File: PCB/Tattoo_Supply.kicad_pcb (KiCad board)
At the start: 4 copper layers, 95 x 128 mm, 140 parts, among them J1 Barrel_Jack_Switch, J2 Out_{1}, J3 Out_{2}, J4 USB_C_Receptacle_USB2.0, J5 Conn_ST_STDC14, J6 Debug_JTAG, J7 Debug_UART, J8 Footswitch, Q1 SiA441DJ, Q2 SSM6J507NU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

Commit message: routage en cours
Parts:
- moved R17 1.68 mm to (119.0, 78.8)
- moved R20 1.68 mm to (119.0, 80.2)
- moved R25 1.68 mm to (119.0, 77.2)
- moved FB1 1.60 mm to (139.2, 69.7), turned to -90 degrees
- moved C1 1.40 mm to (87.0, 62.8)
- moved D3 1.40 mm to (87.0, 61.0)
- moved C33 1.25 mm to (127.5, 116.0)
- moved R41 1.25 mm to (126.0, 116.0)
- moved R18 1.20 mm to (123.6, 77.7)
- moved R19 1.20 mm to (123.6, 79.2)
- moved R9 1.15 mm to (91.0, 73.2)
- moved C17 1.10 mm to (119.4, 68.0), turned to 90 degrees
- moved C31 0.93 mm to (126.0, 112.8), turned to -90 degrees
- moved C14 0.89 mm to (130.4, 62.4)
- moved C20 0.29 mm to (126.6, 78.0), turned to 180 degrees
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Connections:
- net Net-(#FLG01-pwr) renamed /USB C Power Delivery/VBUS_USB
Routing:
- net +3V3: track 0.00 -> 88.7 mm, vias 0 -> 23
- net GND: track 6.21 -> 58.4 mm, vias 3 -> 19
- net /USB C Power Delivery/VBUS_USB: track 2.46 -> 18.9 mm, vias 0 -> 8
- net /MCU/~{RESET}: track 0.00 -> 15.9 mm
- net /MCU/OSC_{IN}: track 0.00 -> 14.3 mm
- net VBUS: track 0.00 -> 12.9 mm, vias 0 -> 15
- net /IO/Handswitch: track 0.00 -> 11.6 mm
- net /BUS_{I2C}.SDA: track 0.00 -> 10.1 mm
- net /MCU/VDDA: track 0.00 -> 9.35 mm
- net /BUS_{I2C}.SCL: track 0.00 -> 8.83 mm
- net Net-(C16-Pad1): track 0.00 -> 8.05 mm
- net /MCU/USB_DFU: track 0.00 -> 7.35 mm
- net Net-(U3-PB13): track 0.00 -> 7.20 mm
- net /MCU/SWCLK: track 0.00 -> 7.10 mm
- net Net-(U3-BOOT0): track 0.00 -> 6.83 mm
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- added copper zone on In1.Cu, net +3V3
- added copper zone on F.Cu, net /USB C Power Delivery/VBUS_USB
- added copper zone on In1.Cu, net /USB C Power Delivery/VBUS_USB
- added copper zone on In2.Cu, net GNDA
- added copper zone on F.Cu, net VBUS
- added copper zone on In1.Cu, net VBUS

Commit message: ok route smps
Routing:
- net /Out Power Control 2/V_{IN}: track 0.00 -> 39.7 mm
- net /Out Power Control 1/V_{IN}: track 0.00 -> 37.4 mm
- net GND: track 58.4 -> 81.9 mm, vias 19 -> 27
- net Net-(U2-FB): track 0.00 -> 8.13 mm
- net Net-(U4-FB): track 0.00 -> 8.13 mm
- net /IO/Footswitch: track 0.00 -> 7.84 mm
- net Net-(U8-IN): track 0.00 -> 6.46 mm
- net Net-(U6-IN): track 0.00 -> 6.36 mm
- net Net-(Q4-G): track 0.00 -> 3.79 mm
- net Net-(Q3-G): track 0.00 -> 3.79 mm
- net /V_{SMPS}2: track 0.00 -> 2.97 mm
- net /V_{SMPS}1: track 0.00 -> 2.97 mm
- net Net-(D12-K): track 0.00 -> 2.70 mm
- net Net-(D10-K): track 0.00 -> 2.70 mm
- net Net-(U8-IS): track 0.00 -> 2.28 mm
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- added copper zone on F.Cu, net /Out Power Control 1/V_{IN}
- added copper zone on F.Cu, net /Out Power Control 1/V_{OUT}
- added copper zone on F.Cu, net /Out Power Control 2/V_{IN}
- added copper zone on F.Cu, net /Out Power Control 2/V_{OUT}
- added copper zone on F.Cu, net GND
- added copper zone on F.Cu, net Net-(D6-K)
- added copper zone on F.Cu, net Net-(D7-K)

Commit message: routage ecran
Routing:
- net /SW2: track 0.00 -> 182.6 mm, vias 0 -> 2
- net /IO/Footswitch: track 7.84 -> 163.2 mm
- net /SW1: track 0.00 -> 145.1 mm, vias 0 -> 2
- net /V_{SMPS}2: track 2.97 -> 130.3 mm, vias 0 -> 2
- net /IO/Encod.DT: track 5.02 -> 97.9 mm, vias 0 -> 2
- net /V_{SMPS}1: track 2.97 -> 93.1 mm, vias 0 -> 2
- net /IO/Encod.CLK: track 5.02 -> 91.3 mm, vias 0 -> 2
- net /IO/Encod.SW: track 6.19 -> 87.6 mm, vias 0 -> 2
- net Net-(JP1-C): track 0.00 -> 77.3 mm, vias 0 -> 2
- net /MCU/SWCLK: track 7.10 -> 70.9 mm, vias 0 -> 2
- net /MCU/SWDIO: track 6.57 -> 66.7 mm, vias 0 -> 2
- net /IO/OLED_{RES}: track 0.00 -> 57.1 mm, vias 0 -> 2
- net /IO/Handswitch: track 11.6 -> 68.6 mm
- net /IO/OLED.~{CS}: track 0.00 -> 54.0 mm, vias 0 -> 2
- net /IO/OLED.SCK: track 0.00 -> 50.2 mm, vias 0 -> 2
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
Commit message: almost done routing
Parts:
- added REF**: Symbol_Barrel_Polarity, Symbol:Symbol_Barrel_Polarity, F.Cu at (109.2, 52.8)
- added REF**: WEEE-Logo_8.4x12mm_SilkScreen, Symbol:WEEE-Logo_8.4x12mm_SilkScreen, B.Cu at (79.6, 169.0)
- moved R5 3.03 mm to (78.2, 65.6)
- moved C1 0.80 mm to (87.8, 62.8)
- moved D3 0.80 mm to (87.8, 61.0)
- moved D2 0.52 mm to (82.8, 64.8), turned to 90 degrees
- moved D4 0.51 mm to (82.8, 60.6), turned to 90 degrees
- moved R39 0.15 mm to (132.8, 116.4)
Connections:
- D2 pad 1: /USB C Power Delivery/CC1 -> /USB C Power Delivery/CC2
- D2 pad 2: /USB C Power Delivery/CC2 -> /USB C Power Delivery/CC1
- D4 pad 1: /BUS_{USB}.D- -> /BUS_{USB}.D+
- D4 pad 2: /BUS_{USB}.D+ -> /BUS_{USB}.D-
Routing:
- net /EN_{SMPS}: track 4.38 -> 132.1 mm, vias 0 -> 3
- net /MCU/Debug.Rx: track 0.00 -> 127.0 mm, vias 0 -> 2
- net /MCU/Debug.Tx: track 0.00 -> 115.5 mm, vias 0 -> 2
- net /BUS_{I2C}.SCL: track 8.83 -> 106.2 mm, vias 0 -> 3
- net /BUS_{I2C}.SDA: track 10.1 -> 101.7 mm, vias 0 -> 3
- net /MCU/~{RESET}: track 26.3 -> 106.1 mm, vias 2 -> 4
- net /V_{DAC}2: track 0.00 -> 74.1 mm, vias 0 -> 2
- net /IO/SW_LED: track 0.00 -> 58.8 mm, vias 0 -> 2
- net /BUS_{USB}.D+: track 0.00 -> 58.1 mm, vias 0 -> 2
- net /BUS_{USB}.D-: track 0.00 -> 56.6 mm, vias 0 -> 2
- net /V_{DAC}1: track 0.00 -> 23.6 mm, vias 0 -> 2
- net GND: track 81.9 -> 91.5 mm, vias 27 -> 47
- net Net-(D6-K): track 0.00 -> 4.55 mm
- net Net-(D7-K): track 0.00 -> 4.55 mm
- net /USB C Power Delivery/VBUS_USB: track 18.9 -> 22.8 mm
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- added copper zone on B.Cu, net GND
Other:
- board text added: "+"
- board text added: "-"
- board text added: "3V3"
- board text added: "DFU"
- board text added: "Debug"
- board text added: "Designed by axoulc V1.0 3-12-2023"
- board text added: "Footswitch"
- board text added: "GND"
- board text added: "OFF"
- board text added: "ON"
- board text added: "OUT1"
- board text added: "OUT2"
- board text added: "Reset"
- board text added: "Rx"
- board text added: "SWCLK"
- board text added: "SWDIO"
- board text added: "Tx"
- board text added: "UART"

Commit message: done V1.0 + gerber + 3d
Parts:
- moved C13 81.2 mm to (54.7, 61.1), turned to 0 degrees
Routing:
- net /MCU/~{RESET}: track 106.1 -> 99.3 mm, vias 4 -> 2
- net GND: track 91.5 -> 89.1 mm, vias 47 -> 86
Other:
- board text added: "24V_{DC} Max."
- board text added: "USB PD 100W Max."

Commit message: Release V1.0
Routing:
- net GND: track 89.1 -> 93.8 mm
- net /EN_{SMPS}: track 132.1 -> 129.6 mm

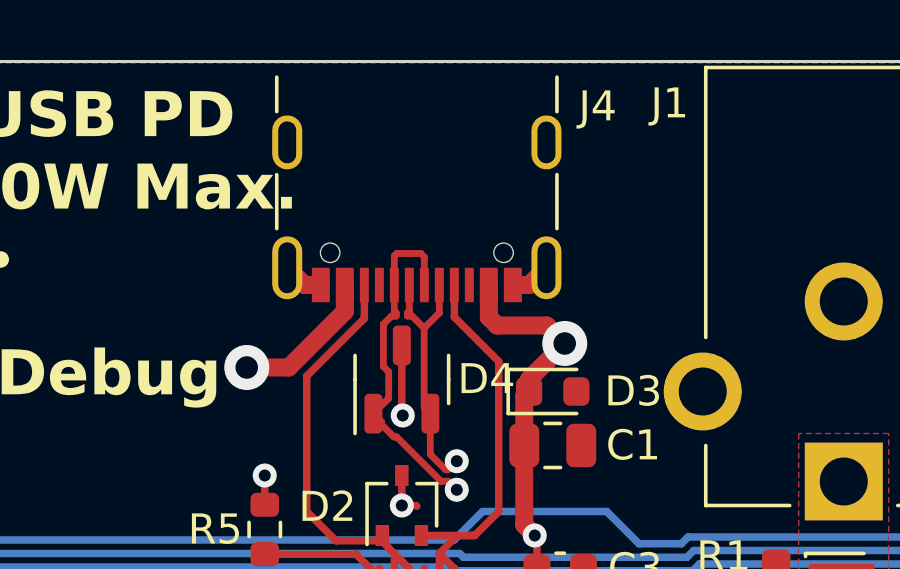
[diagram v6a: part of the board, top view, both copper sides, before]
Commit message: switch kicad 8 and change USB connector
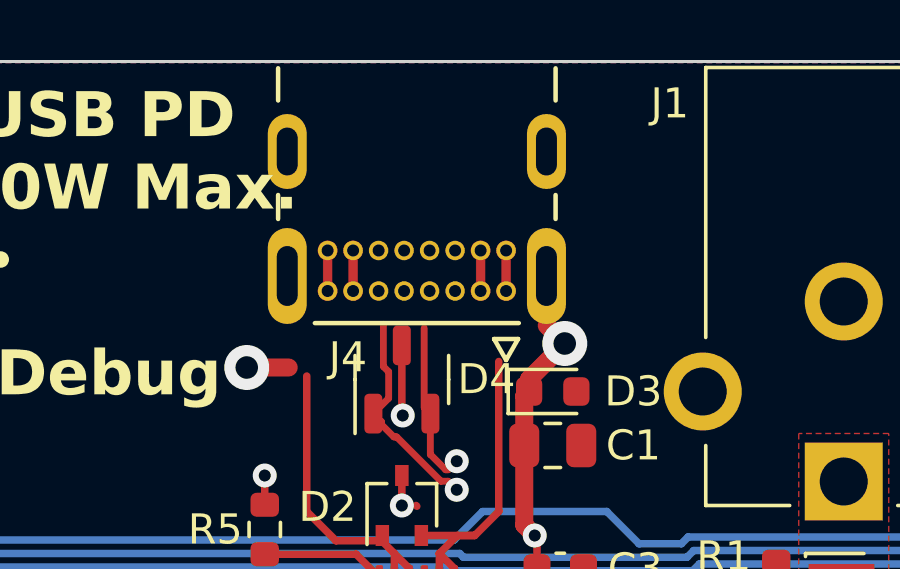
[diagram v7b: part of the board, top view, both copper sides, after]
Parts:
- J4: footprint Connector_USB:USB_C_Receptacle_GCT_USB4105-xx-A_16P_TopMnt_Horizontal -> TattooSupplyFootprints:MOLEX_2137160001
- moved J4 3.77 mm to (83.3, 50.0)
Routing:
- net /USB C Power Delivery/VBUS_USB: track 22.8 -> 16.1 mm
- net /BUS_{USB}.D+: track 58.1 -> 53.4 mm
- net /USB C Power Delivery/CC2: track 13.7 -> 9.82 mm
- net /BUS_{USB}.D-: track 56.6 -> 53.1 mm
- net /USB C Power Delivery/CC1: track 14.3 -> 11.1 mm
- net GND: track 93.8 -> 91.1 mm
